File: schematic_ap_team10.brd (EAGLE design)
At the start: 47 x 28 mm, 47 parts, among them J1 FTDI_DEVICE, M1 WIRELESS-NRF24L01, U1 ATMEGA328P_TQFP, U2 GY-521MPU6050

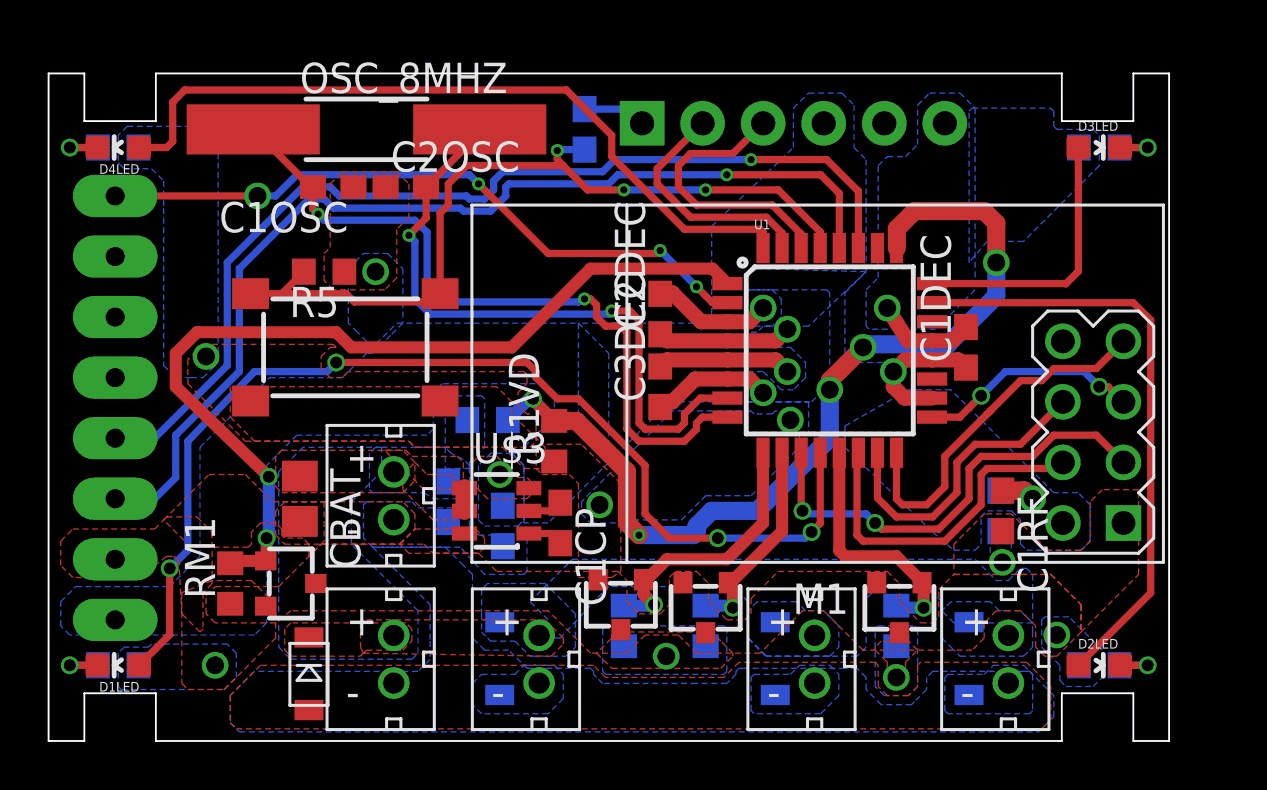
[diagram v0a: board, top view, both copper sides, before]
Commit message: 5th Draft
Changed the layout to have JSTs on the side
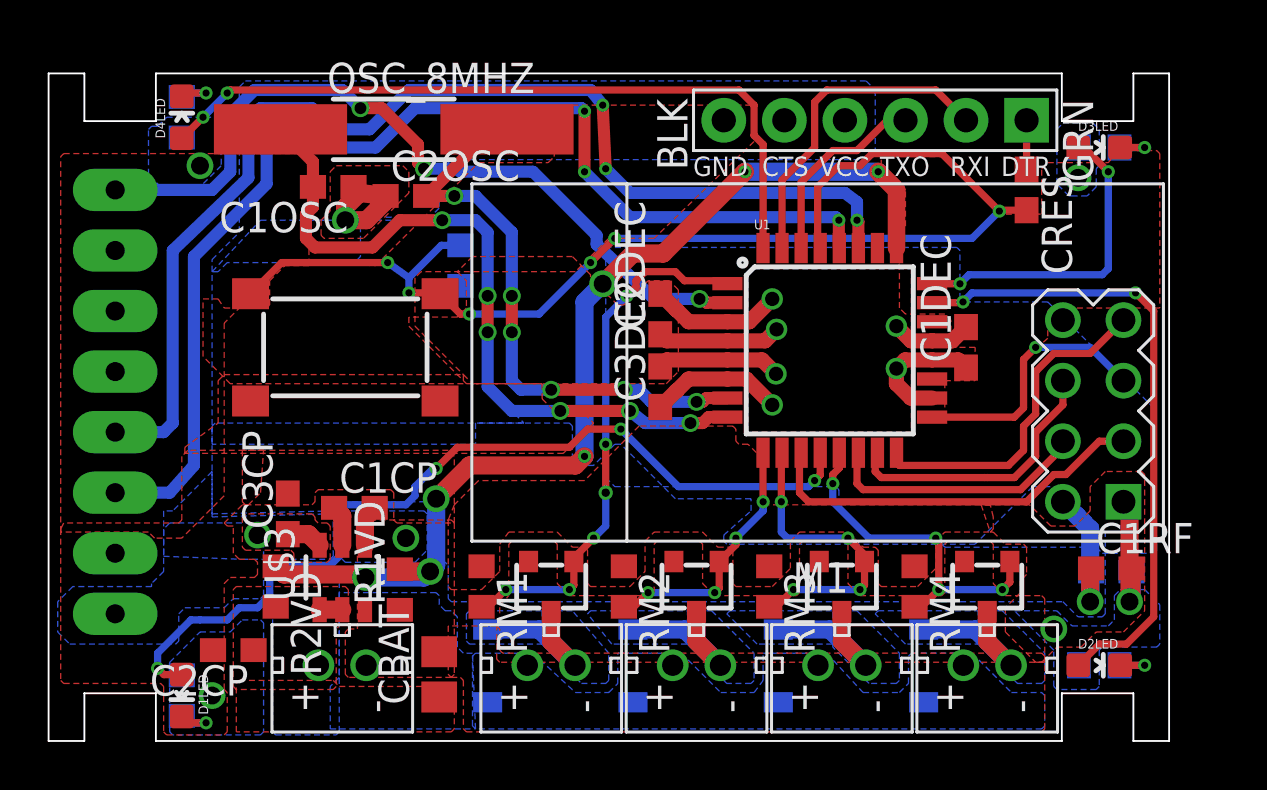
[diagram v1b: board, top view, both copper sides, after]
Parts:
- moved CRES 18.7 mm to (41.0, 23.1), flipped to the top
- moved R2VD 11.3 mm to (9.53, 6.48), flipped to the top, turned to 270 degrees
- moved C2CP 11.0 mm to (7.75, 3.81), flipped to the top, turned to 180 degrees
- moved U$1 10.9 mm to (21.1, 6.48), turned to 180 degrees
- moved RM1 10.5 mm to (18.2, 6.48), turned to 270 degrees
- moved CBAT 9.40 mm to (16.4, 2.79), turned to 90 degrees
- moved C3CP 9.03 mm to (10.0, 9.53), flipped to the top, turned to 90 degrees
- moved R1VD 8.98 mm to (14.7, 6.35)
- moved C1CP 8.66 mm to (12.8, 9.78), turned to 0 degrees
- moved DM1 7.50 mm to (18.4, 3.17), flipped to the bottom, turned to 180 degrees
- moved U$11 7.43 mm to (12.3, 3.17), turned to 90 degrees
- moved U$3 7.05 mm to (12.3, 6.86), turned to 90 degrees
- moved U$4 6.61 mm to (21.1, 3.17), turned to 90 degrees
- moved U$5 6.61 mm to (27.2, 3.17), turned to 90 degrees
- moved U$6 5.78 mm to (33.3, 6.48)
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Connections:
- net 3V3 renamed DVCC
- net VBAT renamed MVCC
- new net N$1: DM1.POS, U$1.3, U$4.-
- new net N$2: DM2.POS, U$2.3, U$5.-
- new net N$4: DM3.POS, U$6.3, U$7.-
- new net N$5: DM4.POS, U$8.3, U$9.-
- net GND: no longer DM1.POS, DM2.POS, DM3.POS, DM4.POS, U$1.3, U$2.3, U$4.-, U$5.-, U$6.3, U$7.-, U$8.3, U$9.-
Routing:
- net RESET: track 33.9 -> 50.8 mm, vias 3 -> 6
- net PWM1: track 37.3 -> 22.3 mm, vias 2 -> 6
- net DVCC: track 19.5 -> 30.4 mm
- net LED1: track 45.8 -> 37.4 mm
- net N$4: track 0.00 -> 6.95 mm
- net N$2: track 0.00 -> 6.95 mm
- net N$1: track 0.00 -> 6.95 mm
- net N$5: track 0.00 -> 6.95 mm
- net SDA: track 42.1 -> 48.7 mm, vias 1 -> 3
- net GND: track 15.2 -> 21.3 mm, vias 11 -> 9
- net SCL: track 42.8 -> 48.8 mm, vias 1 -> 3
- net INT: track 28.4 -> 33.2 mm, vias 4 -> 3
- net PWM4: track 10.4 -> 14.6 mm, vias 1 -> 4
- net PWM3: track 8.76 -> 12.9 mm, vias 1 -> 4
- net VDIV: track 38.8 -> 42.9 mm, vias 5 -> 7
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- added copper zone on layer 16, net N$1
- added copper zone on layer 16, net N$2
- added copper zone on layer 16, net N$4
- added copper zone on layer 16, net N$5

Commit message: Actual 5th (final?) Draft
Changed some parts as well (the oscillator) and moved stuff around.
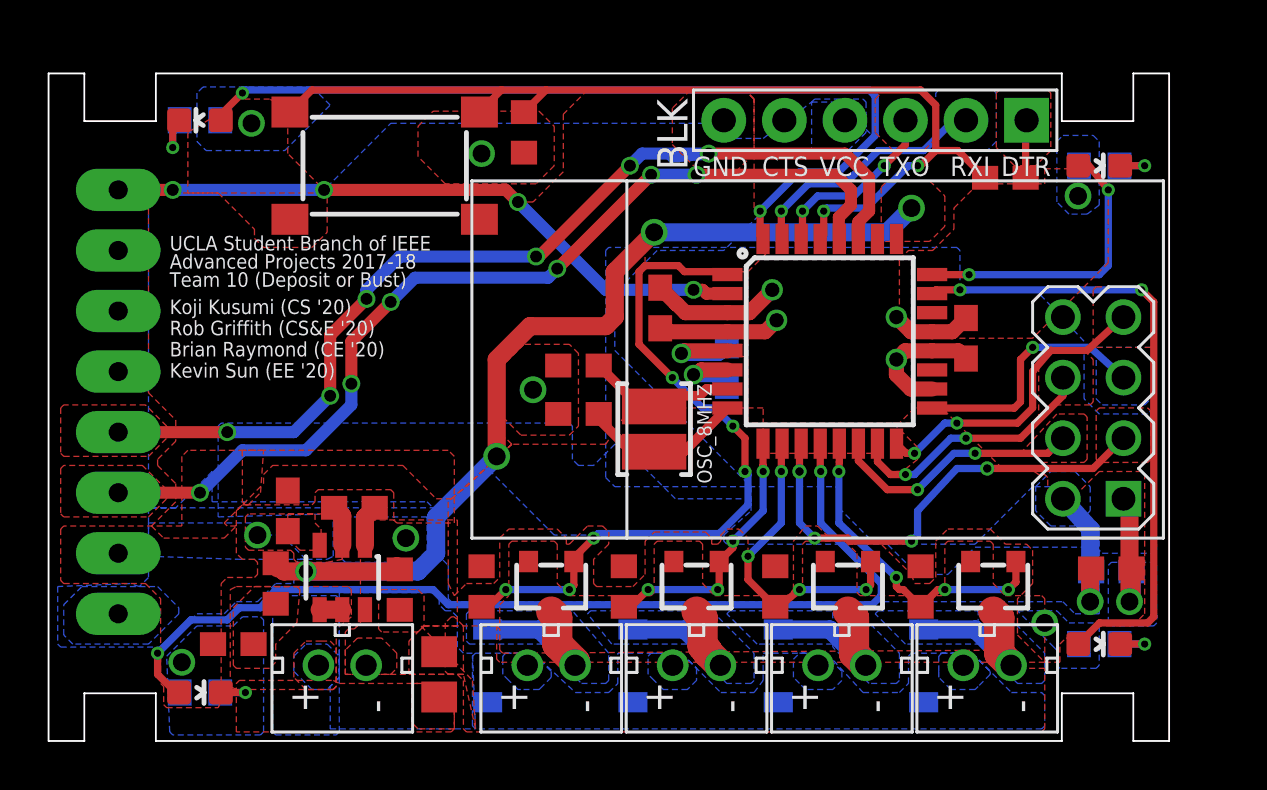
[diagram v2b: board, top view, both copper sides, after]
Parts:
- C1OSC, C2OSC: value 30 pF -> 10 pF
- OSC_8MHZ: value ABLSB4-T -> NX3225GD; device ABLS_B4_T:SOT-23 -> NX3225GD:2-SMD
- moved OSC_8MHZ 16.7 mm to (25.4, 13.1), turned to 90 degrees
- moved C1OSC 14.0 mm to (22.2, 13.7), turned to 0 degrees
- moved C2OSC 10.1 mm to (22.2, 15.7)
- moved U$10 7.80 mm to (14.1, 24.1)
- moved R5 6.19 mm to (19.9, 25.5), flipped to the top
- moved C3DEC 2.93 mm to (28.4, 15.7), flipped to the bottom
- moved CRES 1.02 mm to (40.1, 23.6), turned to 180 degrees
- moved D2LED 0.89 mm to (44.1, 4.06)
- moved R2LED 0.89 mm to (44.1, 4.06)
- moved D1LED 0.77 mm to (6.35, 2.03), turned to 270 degrees
- moved R1LED 0.77 mm to (6.35, 2.03), turned to 180 degrees
- moved D4LED 0.77 mm to (6.35, 26.0), turned to 90 degrees
- moved R4LED 0.77 mm to (6.35, 26.0), turned to 0 degrees
- moved D3LED 0.76 mm to (44.1, 24.1)
- moved R3LED 0.76 mm to (44.1, 24.1)
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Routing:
- net TOSC2: track 31.0 -> 7.21 mm, vias 6 -> 0
- net TOSC1: track 25.3 -> 6.41 mm, vias 6 -> 0
- net DVCC: track 30.4 -> 21.2 mm, vias 6 -> 7
- net RESET: track 50.8 -> 42.1 mm, vias 6 -> 2
- net SCL: track 48.8 -> 40.4 mm, vias 3 -> 6
- net PWM1: track 22.3 -> 29.6 mm
- net SDA: track 48.7 -> 42.7 mm, vias 3 -> 6
- net LED4: track 31.3 -> 37.2 mm
- net INT: track 33.2 -> 27.4 mm, vias 3 -> 4
- net LED1: track 37.4 -> 41.7 mm, vias 4 -> 2
- net TX: track 13.8 -> 10.5 mm, vias 0 -> 1
- net CE: track 16.5 -> 19.7 mm, vias 0 -> 4
- net MISO: track 14.1 -> 13.0 mm, vias 0 -> 2
- net N$19: track 2.16 -> 3.23 mm
- net VDIV: track 42.9 -> 41.8 mm, vias 7 -> 4
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- added copper zone on layer 1, net CE
- added copper zone on layer 1, net CSN
- added copper zone on layer 1, net MISO
- added copper zone on layer 1, net MOSI
- added copper zone on layer 1, net N$3
- added copper zone on layer 1, net RX
- added copper zone on layer 16, net SCK
- added copper zone on layer 1, net SCL
- added copper zone on layer 1, net SDA
- added copper zone on layer 16, net TX
- added copper zone on layer 1, net VDIV
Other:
- board text added: "Advanced Projects 2017-18"
- board text added: "Brian Raymond (CE '20)"
- board text added: "Kevin Sun (EE '20)"
- board text added: "Koji Kusumi (CS '20)"
- board text added: "Rob Griffith (CS&E '20)"
- board text added: "Team 10 (Deposit or Bust)"
- board text added: "UCLA Student Branch of IEEE"
